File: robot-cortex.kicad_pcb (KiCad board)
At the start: 4 copper layers, 27.5 x 26.9 mm, 77 parts, among them J1 USB4110GFA, M1 THRU_HOLE_PAD, M2 THRU_HOLE_PAD, Q1 SS8050-G, Q2 SS8050-G, U1 C2901617, U10 TPS63070, U11 TPS63070, U2 STM32G431CBT6, U3 TLE9250XSJXUMA1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

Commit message: gnd review
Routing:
- net /VDD_MIXED: track 33.3 -> 31.9 mm
- net GND: vias 37 -> 45

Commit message: some shuffling
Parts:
- moved C5 0.89 mm to (203.8, 107.3), turned to 180 degrees
- moved U3 0.34 mm to (199.0, 109.3)
- moved C22 0.22 mm to (190.8, 113.2)
- moved C23 0.22 mm to (193.9, 114.9)
- moved C24 0.22 mm to (197.4, 111.3)
- moved C31 0.22 mm to (197.4, 113.8)
- moved C32 0.22 mm to (196.3, 111.3)
- moved C33 0.22 mm to (196.3, 113.8)
- moved L1 0.22 mm to (193.0, 110.0)
- moved R13 0.22 mm to (195.3, 113.2)
- moved R14 0.22 mm to (195.3, 114.6)
- moved R15 0.22 mm to (192.8, 115.3)
- moved U11 0.22 mm to (193.1, 112.9)
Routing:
- net /+5V0: track 37.2 -> 45.4 mm
- net /ESP32/RTS: track 17.0 -> 18.4 mm, vias 3 -> 2
- net +3V3: track 51.8 -> 53.2 mm
- net /VDD_MIXED: track 31.9 -> 31.5 mm, vias 4 -> 5
- net GND: vias 45 -> 47

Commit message: labeleled
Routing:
- net GND: vias 47 -> 62
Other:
- board text added: "3V3"
- board text added: "CH"
- board text added: "CL"
- board text added: "EN"
- board text added: "GND"
- board text added: "IO0"
- board text added: "RX"
- board text added: "SWCLK"
- board text added: "SWDIO"
- board text added: "TCK"
- board text added: "TDI"
- board text added: "TDO"
- board text added: "TMS"
- board text added: "TX"
- board text added: "VBAT"
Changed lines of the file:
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@@
   (gr_line (start 217.5 90.1) (end 217.5 116)
     (stroke (width 0.1) (type default)) (layer "Edge.Cuts"))
+  (gr_text "SWDIO" (at 211.92 93.22 90) (layer "B.SilkS")
+    (effects (font (size 0.762 0.762) (thickness 0.127)) (justify left bottom mirror))
+  )
+  (gr_text "SWCLK" (at 213.28 93.22 90) (layer "B.SilkS")
+    (effects (font (size 0.762 0.762) (thickness 0.127)) (justify left bottom mirror))
+  )
+  (gr_text "3V3" (at 195.8 104.21) (layer "B.SilkS")
+    (effects (font (size 0.635 0.635) (thickness 0.127)) (justify left bottom mirror))
+  )
+  (gr_text "TX" (at 217.36 111.95 90) (layer "B.SilkS")
+    (effects (font (size 0.635 0.635) (thickness 0.127)) (justify left bottom mirror))
+  )
+  (gr_text "VBAT" (at 194.94 112.13) (layer "B.SilkS")
+    (effects (font (size 0.635 0.635) (thickness 0.127)) (justify left bottom mirror))
+  )
+  (gr_text "IO0" (at 195.8 102.07) (layer "B.SilkS")
+    (effects (font (size 0.635 0.635) (thickness 0.127)) (justify left bottom mirror))
+  )
+  (gr_text "GND" (at 195.15 107.64) (layer "B.SilkS")
+    (effects (font (size 0.635 0.635) (thickness 0.127)) (justify left bottom mirror))
+  )
+  (gr_text "CL" (at 195.39 110.46) (layer "B.SilkS")
+    (effects (font (size 0.635 0.635) (thickness 0.127)) (justify left bottom mirror))
+  )
+  (gr_text "TDI" (at 195.8 99.12) (layer "B.SilkS")
+    (effects (font (size 0.635 0.635) (thickness 0.127)) (justify left bottom mirror))
+  )
+  (gr_text "GND" (at 195.8 97.07) (layer "B.SilkS")
+    (effects (font (size 0.635 0.635) (thickness 0.127)) (justify left bottom mirror))
+  )
+  (gr_text "RX" (at 217.36 114.49 90) (layer "B.SilkS")
+    (effects (font (size 0.635 0.635) (thickness 0.127) bold) (justify left bottom mirror))
+  )
+  (gr_text "TDO" (at 195.8 101.06) (layer "B.SilkS")
+    (effects (font (size 0.635 0.635) (thickness 0.127)) (justify left bottom mirror))
+  )
+  (gr_text "CH" (at 195.42 109.12) (layer "B.SilkS")
+    (effects (font (size 0.635 0.635) (thickness 0.127)) (justify left bottom mirror))
+  )
+  (gr_text "TMS" (at 195.8 100.09) (layer "B.SilkS")
+    (effects (font (size 0.635 0.635) (thickness 0.127)) (justify left bottom mirror))
+  )
+  (gr_text "TCK" (at 195.8 98.17) (layer "B.SilkS")
+    (effects (font (size 0.635 0.635) (thickness 0.127)) (justify left bottom mirror))
+  )
+  (gr_text "GND" (at 214.54 93.28 90) (layer "B.SilkS")
+    (effects (font (size 0.762 0.762) (thickness 0.127)) (justify left bottom mirror))
+  )
+  (gr_text "EN" (at 195.8 103.09) (layer "B.SilkS")
+    (effects (font (size 0.635 0.635) (thickness 0.127)) (justify left bottom mirror))
+  )
   (segment (start 215.55 95.65) (end 215.55 94.23) (width 0.381) (layer "F.Cu") (net 1))
   (segment (start 214.555 93.94) (end 215.26 93.94) (width 0.3048) (layer "F.Cu") (net 1))
@@
   (via (at 193.3 107.5) (size 0.45) (drill 0.2) (layers "F.Cu" "B.Cu") (net 2))
   (via (at 201.45 105.03) (size 0.45) (drill 0.2) (layers "F.Cu" "B.Cu") (net 2))
+  (via (at 212.76 90.87) (size 0.45) (drill 0.2) (layers "F.Cu" "B.Cu") (net 2))
   (via (at 206.21 116) (size 0.45) (drill 0.2) (layers "F.Cu" "B.Cu") (net 2))
   (via (at 194.4 106.4) (size 0.45) (drill 0.2) (layers "F.Cu" "B.Cu") (net 2))
@@
   (via (at 190.91 100.12) (size 0.45) (drill 0.2) (layers "F.Cu" "B.Cu") (net 2))
   (via (at 199.57 115.68) (size 0.45) (drill 0.2) (layers "F.Cu" "B.Cu") (net 2))
+  (via (at 213.45 115.1) (size 0.45) (drill 0.2) (layers "F.Cu" "B.Cu") (net 2))
+  (via (at 214.895369 92.253993) (size 0.45) (drill 0.2) (layers "F.Cu" "B.Cu") (net 2))
   (via (at 200.4 109.52) (size 0.45) (drill 0.2) (layers "F.Cu" "B.Cu") (net 2))
+  (via (at 203.28 93.76) (size 0.45) (drill 0.2) (layers "F.Cu" "B.Cu") (net 2))
   (via (at 205.58 116.01) (size 0.45) (drill 0.2) (layers "F.Cu" "B.Cu") (net 2))
   (via (at 194.23 107.24) (size 0.45) (drill 0.2) (layers "F.Cu" "B.Cu") (net 2))
   (via (at 195.165129 94.734871) (size 0.45) (drill 0.2) (layers "F.Cu" "B.Cu") (net 2))
+  (via (at 204.07 92.62) (size 0.45) (drill 0.2) (layers "F.Cu" "B.Cu") (net 2))
   (via (at 198.38 115) (size 0.45) (drill 0.2) (layers "F.Cu" "B.Cu") (net 2))
+  (via (at 216.36 104.71) (size 0.45) (drill 0.2) (layers "F.Cu" "B.Cu") (net 2))
   (via (at 216.73 92.77) (size 0.45) (drill 0.2) (layers "F.Cu" "B.Cu") (net 2))
   (via (at 202.3445 99.306107) (size 0.45) (drill 0.2) (layers "F.Cu" "B.Cu") (net 2))
   (via (at 197.6 106.45) (size 0.45) (drill 0.2) (layers "F.Cu" "B.Cu") (net 2))
+  (via (at 202.31 92.71) (size 0.45) (drill 0.2) (layers "F.Cu" "B.Cu") (net 2))
+  (via (at 210.95 92.56) (size 0.45) (drill 0.2) (layers "F.Cu" "B.Cu") (net 2))
+  (via (at 205.17 93.55) (size 0.45) (drill 0.2) (layers "F.Cu" "B.Cu") (net 2))
   (via (at 201.85 105.68) (size 0.45) (drill 0.2) (layers "F.Cu" "B.Cu") (net 2))
   (via (at 201.14 115.2) (size 0.45) (drill 0.2) (layers "F.Cu" "B.Cu") (net 2))
-  (via (at 201.77 106.26) (size 0.45) (drill 0.2) (layers "F.Cu" "B.Cu") (net 2))
+  (via (at 202.61 106.29) (size 0.45) (drill 0.2) (layers "F.Cu" "B.Cu") (net 2))
   (via (at 194.89 107.65) (size 0.45) (drill 0.2) (layers "F.Cu" "B.Cu") (net 2))
+  (via (at 216.36 110.96) (size 0.45) (drill 0.2) (layers "F.Cu" "B.Cu") (net 2))
   (via (at 200.2 97) (size 0.45) (drill 0.2) (layers "F.Cu" "B.Cu") (net 2))
+  (via (at 216.188708 106.610047) (size 0.45) (drill 0.2) (layers "F.Cu" "B.Cu") (net 2))
   (via (at 211.87 115.87) (size 0.45) (drill 0.2) (layers "F.Cu" "B.Cu") (net 2))
   (via (at 206.191619 111.878844) (size 0.45) (drill 0.2) (layers "F.Cu" "B.Cu") (net 2))
@@
   (via (at 197.75 115.31) (size 0.45) (drill 0.2) (layers "F.Cu" "B.Cu") (net 2))
   (via (at 197.56 105.78) (size 0.45) (drill 0.2) (layers "F.Cu" "B.Cu") (net 2))
+  (via (at 215.87 105.62) (size 0.45) (drill 0.2) (layers "F.Cu" "B.Cu") (net 2))
   (via (at 213.79 115.98) (size 0.45) (drill 0.2) (layers "F.Cu" "B.Cu") (net 2))
   (via (at 193.9 108.2) (size 0.45) (drill 0.2) (layers "F.Cu" "B.Cu") (net 2))
+  (via (at 210.454908 99.539798) (size 0.45) (drill 0.2) (layers "F.Cu" "B.Cu") (net 2))
   (via (at 202.01 115) (size 0.45) (drill 0.2) (layers "F.Cu" "B.Cu") (net 2))
   (via (at 211.2 110.36) (size 0.45) (drill 0.2) (layers "F.Cu" "B.Cu") (net 2))
+  (via (at 203.66 106.22) (size 0.45) (drill 0.2) (layers "F.Cu" "B.Cu") (net 2))
   (via (at 190.82 100.98) (size 0.45) (drill 0.2) (layers "F.Cu" "B.Cu") (net 2))
   (via (at 196.7885 97.5) (size 0.45) (drill 0.2) (layers "F.Cu" "B.Cu") (net 2))
   (via (at 190.95 98.91) (size 0.45) (drill 0.2) (layers "F.Cu" "B.Cu") (net 2))
   (via (at 212.87 115.93) (size 0.45) (drill 0.2) (layers "F.Cu" "B.Cu") (net 2))
+  (via (at 216.188708 90.895988) (size 0.45) (drill 0.2) (layers "F.Cu" "B.Cu") (net 2))
   (via (at 197.56 105.15) (size 0.45) (drill 0.2) (layers "F.Cu" "B.Cu") (net 2))
   (via (at 196.96 115.34) (size 0.45) (drill 0.2) (layers "F.Cu" "B.Cu") (net 2))

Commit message: changes that are tested+working
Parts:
- removed C1: 100nF, robot-cortex:C_0402_1005Metric
- added R2: 4.7k, robot-cortex:R_0402_1005Metric, B.Cu at (214.2, 111.1)
- U7: value DF52-5S-0.8H(21) -> DF52-8S-0.8H(21)
- moved D7 2.54 mm to (207.2, 94.0)
- moved R17 2.54 mm to (205.2, 94.0)
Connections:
- U8 pad 6: Net-(D7-A) -> unconnected-(U8-IO34-Pad6)
- U8 pad 8: unconnected-(U8-IO32-Pad8) -> Net-(D7-A)

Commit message: rs485
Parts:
- removed C28, C31: C2998534, robot-cortex:C_0603_1608Metric
- added C1: 100nF, Capacitor_SMD:C_0402_1005Metric, B.Cu at (202.6, 112.3)
- added C36: 100nF, Capacitor_SMD:C_0402_1005Metric, B.Cu at (200.8, 112.3)
- added IC1: THVD2410VDRCR, robot-cortex:THVD2410VDRCR, B.Cu at (201.7, 114.7)
- added R18: 1k, robot-cortex:R_0402_1005Metric, B.Cu at (199.5, 113.7)
- added R19: 120, robot-cortex:R_0402_1005Metric, B.Cu at (198.9, 114.5)
- added R20: 1k, robot-cortex:R_0402_1005Metric, B.Cu at (199.5, 115.2)
- C7: moved to F.Cu
- moved C7 1.76 mm to (205.9, 115.1), turned to 0 degrees
- moved C33 0.43 mm to (196.3, 114.2)
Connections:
- net /CANH renamed /A-PROTECTED
- net /CANL renamed /B-PROTECTED
- U2 pad 30: unconnected-(U2-PA8-Pad30) -> /UART1_DE
- U8 pad 29: /SS -> /ESP32/ESP32_SS
- U8 pad 30: /SPI1_SCK -> /ESP32/ESP32_SCK
- U8 pad 31: /SPI1_MISO -> /ESP32/ESP32_MISO
- U8 pad 37: /SPI1_MOSI -> /ESP32/ESP32_MOSI
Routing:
- net /SPI1_MOSI: track 14.3 -> 0.00 mm, vias 1 -> 0
- net /UART1_TX: track 0.00 -> 11.8 mm, vias 0 -> 2
- net /UART1_RX: track 0.00 -> 11.5 mm
- net /A-PROTECTED: track 3.59 -> 14.9 mm, vias 0 -> 2
- net +3V3: track 53.2 -> 61.0 mm, vias 21 -> 20
- net /B-PROTECTED: track 3.56 -> 11.2 mm, vias 0 -> 2
- net /SPI1_SCK: track 6.69 -> 0.00 mm, vias 1 -> 0
- net /SPI1_MISO: track 6.50 -> 0.00 mm, vias 1 -> 0
- net /UART1_DE: track 0.00 -> 6.42 mm, vias 0 -> 2
- net /+5V0: track 45.4 -> 48.5 mm
- net /ESP32/IO0: track 38.0 -> 38.5 mm, vias 6 -> 5
- net GND: vias 62 -> 55

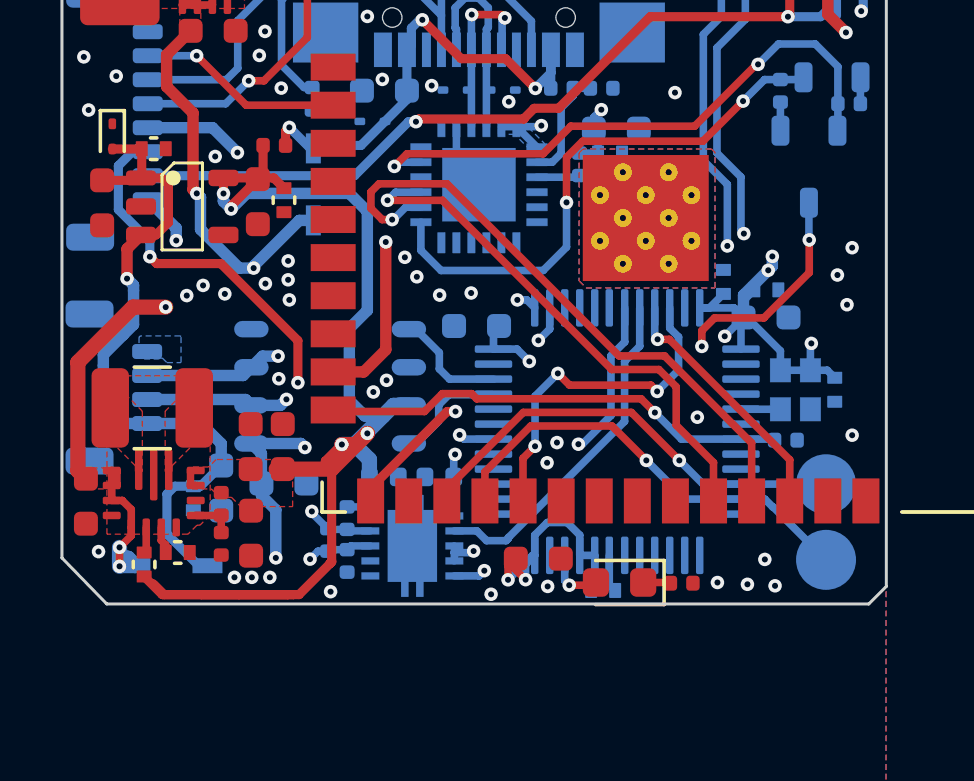
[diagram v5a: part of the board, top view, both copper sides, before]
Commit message: routed but want to reroute differential pairs
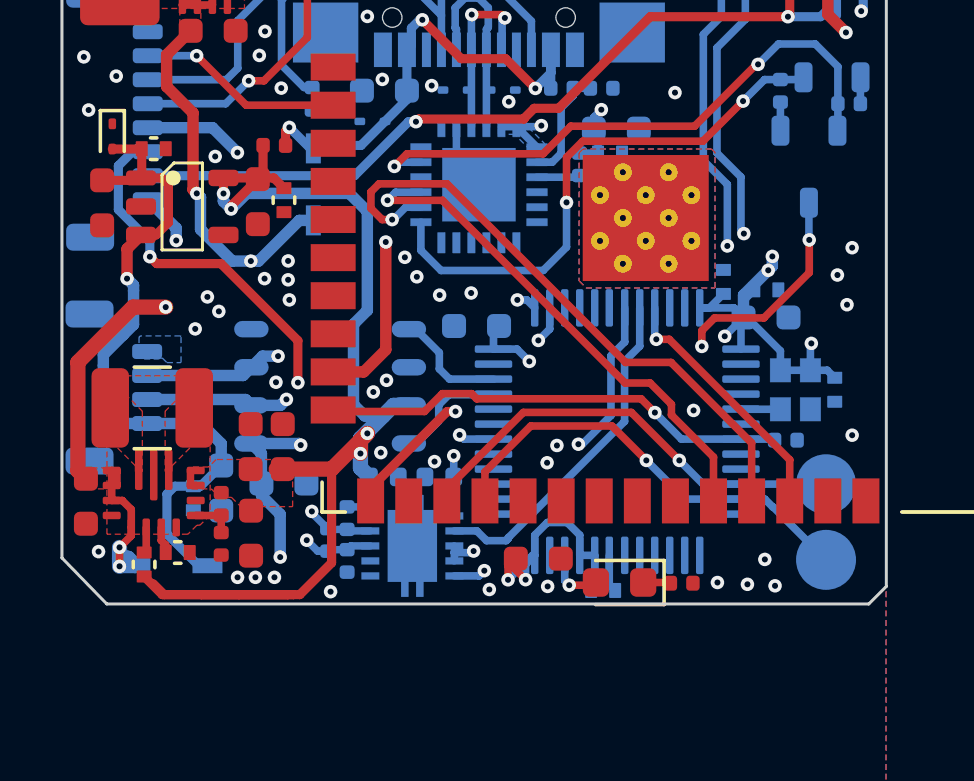
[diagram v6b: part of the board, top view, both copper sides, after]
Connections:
- IC1 pad 8: /A-PROTECTED -> /A-PROTECTED+
- IC1 pad 9: /B-PROTECTED -> /B-PROTECTED-
- R18 pad 1: /B-PROTECTED -> /B-PROTECTED-
- R19 pad 1: /A-PROTECTED -> /A-PROTECTED+
- R19 pad 2: /B-PROTECTED -> /B-PROTECTED-
- R20 pad 2: /A-PROTECTED -> /A-PROTECTED+
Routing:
- net /SS: track 11.5 -> 0.00 mm, vias 3 -> 0
- net /B-PROTECTED: track 11.2 -> 12.4 mm
- net /A-PROTECTED: track 14.9 -> 14.1 mm
- net /VDD_MIXED: track 31.5 -> 31.0 mm
- net GND: vias 55 -> 57

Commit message: rerouted
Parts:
- moved C9 1.34 mm to (196.6, 113.6), turned to -90 degrees
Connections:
- IC1 pad 8: /A-PROTECTED+ -> /C-
- IC1 pad 9: /B-PROTECTED- -> /C+
- R18 pad 1: /B-PROTECTED- -> /C+
- R19 pad 1: /A-PROTECTED+ -> /C-
- R19 pad 2: /B-PROTECTED- -> /C+
- R20 pad 2: /A-PROTECTED+ -> /C-
- U3 pad 6: /B-PROTECTED -> /C-
- U3 pad 7: /A-PROTECTED -> /C+
- U5 pad 2: /B-PROTECTED -> /C-
- U5 pad 3: /A-PROTECTED -> /C+
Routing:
- net /A-PROTECTED: track 14.1 -> 0.00 mm, vias 2 -> 0
- net /B-PROTECTED: track 12.4 -> 0.00 mm, vias 2 -> 0
- net /C+: track 0.00 -> 12.1 mm
- net /C-: track 0.00 -> 11.6 mm
- net +3V3: track 60.7 -> 59.8 mm
- net /ESP32/IO0: track 38.5 -> 37.7 mm
